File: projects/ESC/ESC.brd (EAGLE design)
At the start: 139.7 x 38.1 mm, 91 parts, among them J1 1755529, J2 1755529, J3 1755529, J4 1755529, U1 STM32F405RGT6, U10 CSD88584Q5DCT, U11 CSD88584Q5DCT, U12 CSD88584Q5DCT, U13 CSD88584Q5DCT, U2 CSD88584Q5DCT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

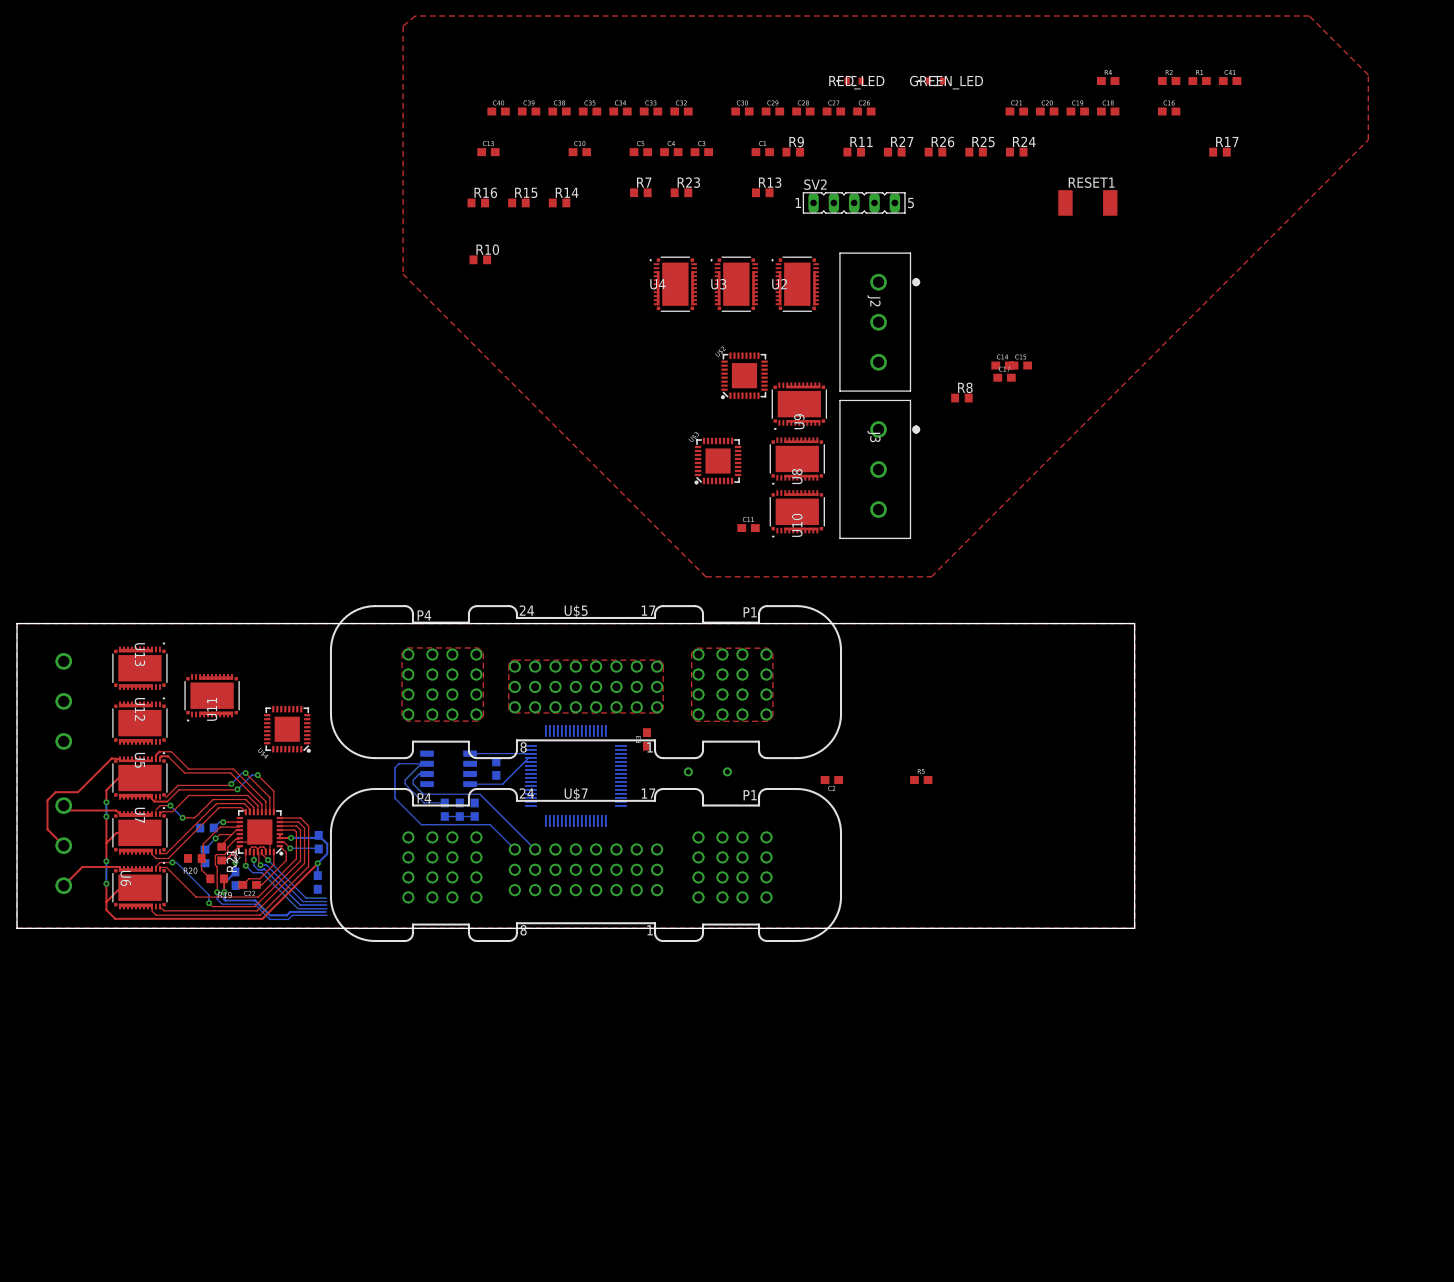
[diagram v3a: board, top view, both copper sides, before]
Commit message: finished the left half of the board
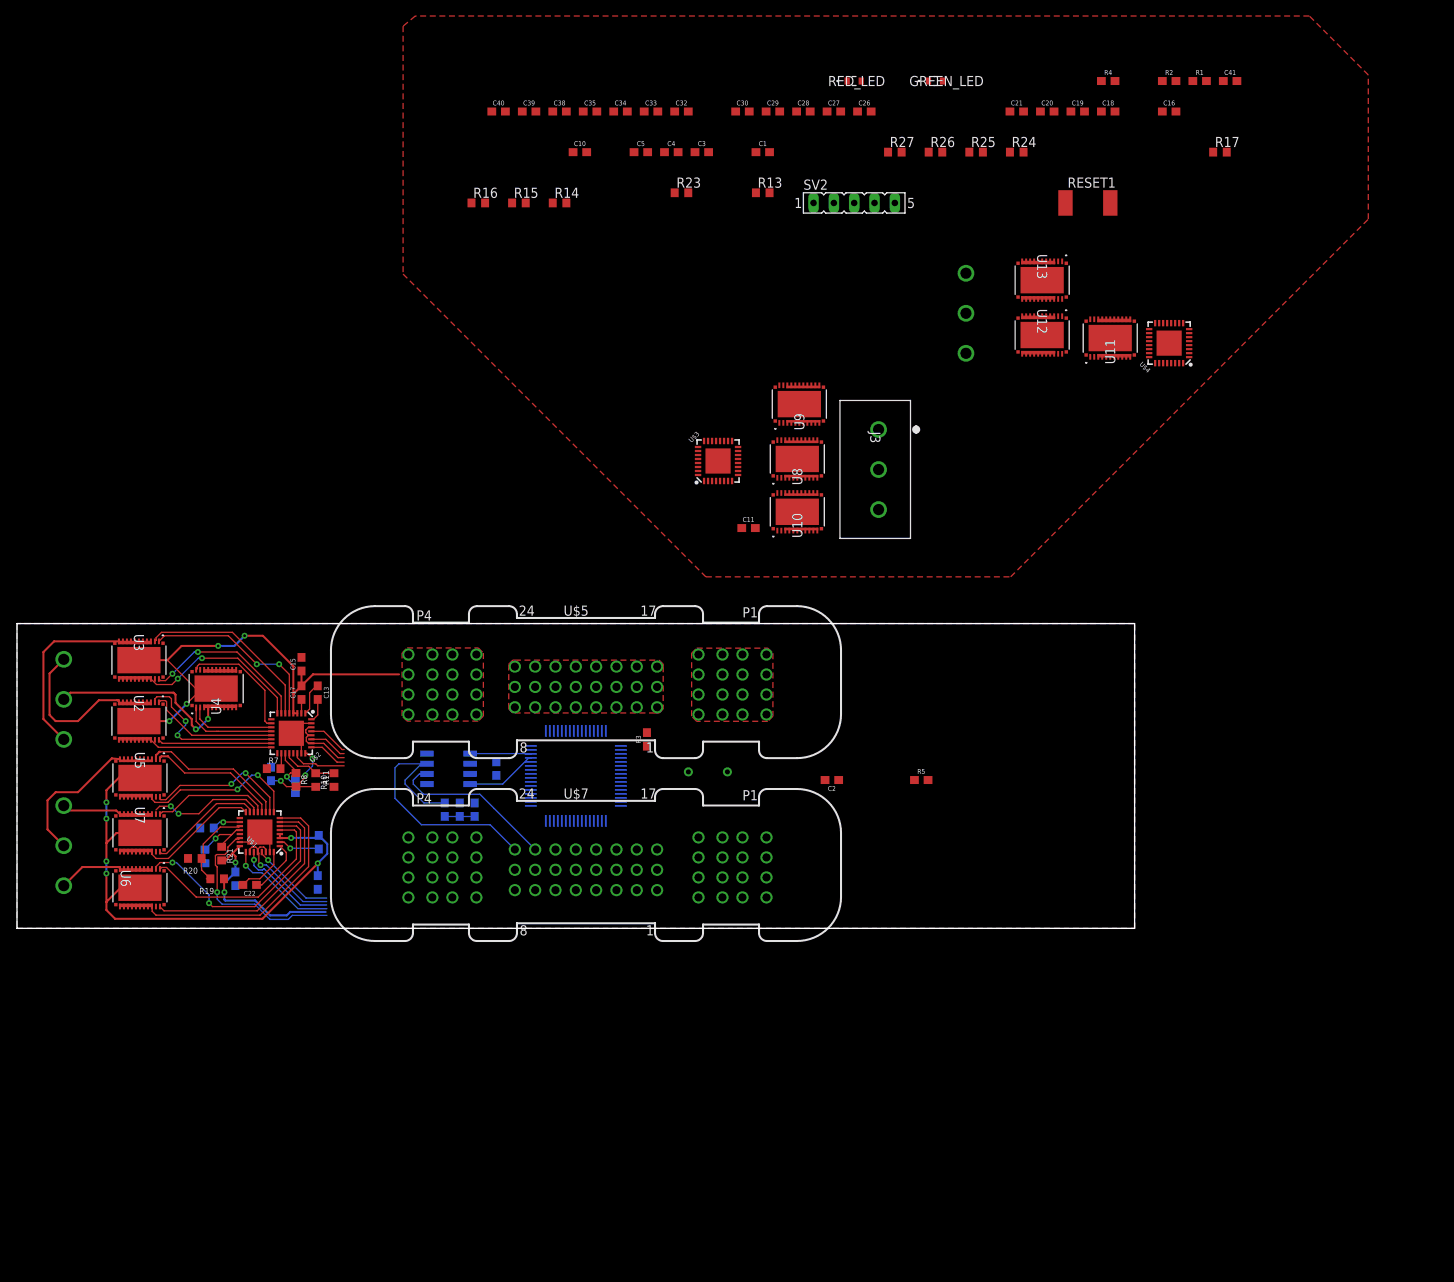
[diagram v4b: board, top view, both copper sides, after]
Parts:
- moved J4 122.8 mm to (118.6, 71.9)
- moved U12 122.8 mm to (128.1, 74.2)
- moved U13 122.8 mm to (128.1, 81.0)
- moved U11 120.8 mm to (136.7, 73.8)
- moved U$4 120.3 mm to (144.0, 73.2)
- moved J2 116.8 mm to (5.84, 23.6), flipped to the bottom, turned to 90 degrees
- moved C14 104.7 mm to (31.8, 19.3), flipped to the bottom, turned to 90 degrees
- moved R11 101.9 mm to (39.6, 18.5), turned to 90 degrees
- moved R9 100.8 mm to (34.8, 17.8), flipped to the bottom, turned to 90 degrees
- moved U2 98.8 mm to (15.2, 25.9), turned to 270 degrees
- moved C15 97.4 mm to (35.6, 33.0), turned to 90 degrees
- moved C17 96.3 mm to (35.6, 29.5), turned to 90 degrees
- moved R8 95.9 mm to (34.9, 18.6), turned to 270 degrees
- moved U3 88.2 mm to (15.2, 33.5), turned to 270 degrees
- moved R7 85.4 mm to (32.1, 20.0)
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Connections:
- removed net N$10: U$2.25
- removed net N$11: U$2.27
- removed net N$14: U$2.29
- removed net N$20: U$3.25
- removed net N$21: U$3.27
- removed net N$22: U$3.29
- net INHA_1: now also U$2.25
- net INHA_3: now also U$3.25
- net INHB_1: now also U$2.27
- net INHB_3: now also U$3.27
- net INHC_1: now also U$2.29
- net INHC_3: now also U$3.29
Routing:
- net VM_1: track 0.00 -> 64.5 mm, vias 0 -> 4
- net PHASE_B1: track 0.00 -> 27.3 mm, vias 0 -> 2
- net PHASE_A1: track 0.00 -> 26.0 mm
- net SLA_1: track 0.00 -> 25.5 mm, vias 0 -> 2
- net GHA_1: track 0.00 -> 23.5 mm, vias 0 -> 2
- net SHA_1: track 0.00 -> 23.2 mm
- net PHASE_C1: track 0.00 -> 21.8 mm
- net GLA_1: track 0.00 -> 21.3 mm, vias 0 -> 2
- net SHC_1: track 0.00 -> 20.4 mm, vias 0 -> 2
- net SLC_1: track 0.00 -> 19.4 mm
- net GHC_1: track 0.00 -> 16.5 mm
- net GLB_1: track 0.00 -> 15.2 mm
- net GLC_1: track 0.00 -> 14.2 mm
- net GHB_1: track 0.00 -> 12.1 mm
- net DVDD_1: track 0.00 -> 11.4 mm, vias 0 -> 3
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
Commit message: Added Fault connection from drvs to stm
forgot to do this earlier
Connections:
- net FAULT_1: now also U$2.17
- net FAULT_2: now also U$1.17
- net FAULT_3: now also U$3.17
- net FAULT_4: now also U$4.17
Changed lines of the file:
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@@
 <?xml version="1.0" encoding="utf-8"?>
 <!DOCTYPE eagle SYSTEM "eagle.dtd">
-<eagle version="9.4.1">
+<eagle version="9.5.1">
 <drawing>
 <settings>
@@
 <signal name="FAULT_1">
 <contactref element="U1" pad="38"/>
+<contactref element="U$2" pad="17"/>
+<wire x1="32.54" y1="21.884" x2="71.1" y2="13.4239" width="0" layer="19" extent="1-16"/>
 </signal>
 <signal name="EN_1">
@@
 <signal name="FAULT_2">
 <contactref element="U1" pad="44"/>
+<contactref element="U$1" pad="17"/>
+<wire x1="27.853" y1="13.7896" x2="68.1" y2="13.4239" width="0" layer="19" extent="1-16"/>
 </signal>
 <signal name="INL_3">
@@
 <signal name="FAULT_3">
 <contactref element="U1" pad="55"/>
+<contactref element="U$3" pad="17"/>
+<wire x1="64.2239" y1="18.3" x2="89.38" y2="60.92" width="0" layer="19" extent="1-16"/>
 </signal>
 <signal name="INHA_4">
@@
 <signal name="FAULT_4">
 <contactref element="U1" pad="28"/>
+<contactref element="U$4" pad="17"/>
+<wire x1="75.4761" y1="17.3" x2="141.518" y2="74.902" width="0" layer="19" extent="1-16"/>
 </signal>
 <signal name="OSC_IN">

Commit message: ERC stuff 1
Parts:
- moved C18 139.1 mm to (116.3, -35.6)
- moved C19 139.1 mm to (112.5, -35.6)
- moved C20 139.1 mm to (108.7, -35.6)
- moved C21 139.1 mm to (104.9, -35.6)
- moved R13 130.6 mm to (121.4, -35.6)
- moved R17 110.9 mm to (113.8, -7.62)
- moved R14 106.3 mm to (76.7, -15.2)
- moved R15 106.3 mm to (71.6, -15.2)
- moved R16 106.3 mm to (66.5, -15.2)
- moved J3 96.8 mm to (141.0, -28.6)
- moved C27 91.3 mm to (107.4, 10.9), turned to 90 degrees
- moved U8 90.1 mm to (128.0, -26.2)
- moved R23 86.2 mm to (126.5, 17.5)
- moved U9 85.5 mm to (119.1, -17.3)
- moved C26 84.5 mm to (119.9, 18.8), turned to 180 degrees
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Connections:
- removed net N$37: U$4.25
- removed net N$38: U$4.27
- removed net N$39: U$4.29
- removed net SLC_1B: U4.12, U4.13, U4.14, U4.15, U4.16, U4.17, U4.18, U4.19, U4.20
- net INHA_4: now also U$4.25
- net INHB_4: now also U$4.27
- net INHC_2: now also U$1.29
- net INHC_3: no longer U$1.29
- net INHC_4: now also U$4.29
- net SLB_1: now also U4.12, U4.13, U4.14, U4.15, U4.16, U4.17, U4.18, U4.19, U4.20
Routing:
- net INHC_3: track 10.6 -> 0.00 mm, vias 1 -> 0
- net INHC_2: track 0.00 -> 10.6 mm, vias 0 -> 1
- net SLC_1B: track 4.00 -> 0.00 mm
- net SLB_1: track 0.00 -> 4.00 mm
- added copper zone on layer 1, net N$10

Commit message: did some layout stuff
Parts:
- moved C28 17.4 mm to (125.2, 22.6)
- moved R23 17.1 mm to (112.0, 26.7), flipped to the bottom, turned to 270 degrees
- moved R25 15.7 mm to (105.2, 31.8), flipped to the bottom, turned to 270 degrees
- moved C27 9.86 mm to (109.5, 20.6), flipped to the bottom, turned to 0 degrees
- moved R27 4.44 mm to (105.2, 21.6), flipped to the bottom, turned to 90 degrees
- moved R26 3.78 mm to (105.2, 24.6), flipped to the bottom, turned to 90 degrees
- moved U12 3.70 mm to (126.2, 29.3), turned to 180 degrees
- moved U13 3.45 mm to (110.7, 33.4), turned to 180 degrees
- moved U11 3.01 mm to (118.5, 31.5), turned to 180 degrees
- moved C29 2.84 mm to (122.9, 22.6)
- moved R24 2.54 mm to (105.2, 28.7), flipped to the bottom
- moved C26 1.44 mm to (120.9, 19.8)
- moved U$4 1.30 mm to (116.1, 22.6)
- moved J4 0.72 mm to (135.1, 23.9)
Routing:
- net VM_4: track 0.00 -> 61.4 mm, vias 0 -> 4
- net PHASE_C4: track 4.00 -> 26.9 mm
- net 12V: track 0.15 -> 18.6 mm
- net INL_4: track 0.00 -> 17.6 mm, vias 0 -> 1
- net EN_4: track 0.00 -> 17.4 mm, vias 0 -> 1
- net SHA_4: track 0.00 -> 17.0 mm
- net INHC_4: track 0.00 -> 16.6 mm, vias 0 -> 1
- net PHASE_B4: track 4.00 -> 20.4 mm
- net FAULT_4: track 0.00 -> 16.1 mm, vias 0 -> 1
- net DVDD_4: track 0.00 -> 15.5 mm, vias 0 -> 1
- net GHA_4: track 0.00 -> 13.5 mm, vias 0 -> 2
- net SLC_4: track 4.00 -> 17.2 mm
- net INHB_4: track 0.00 -> 12.9 mm, vias 0 -> 1
- net N$43: track 0.00 -> 12.6 mm, vias 0 -> 1
- net GLC_4: track 0.00 -> 11.9 mm
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
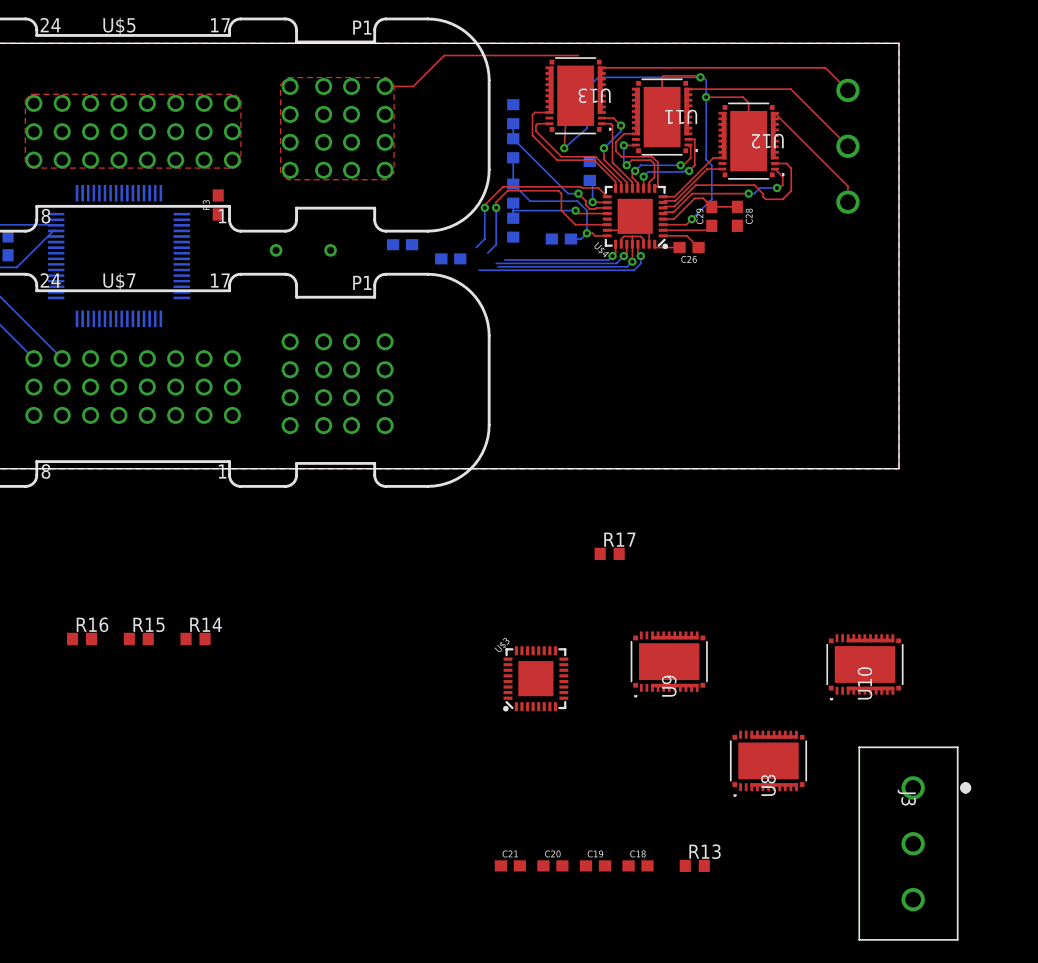
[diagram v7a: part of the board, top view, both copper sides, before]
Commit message: Did the right side of the board (needs polygons)
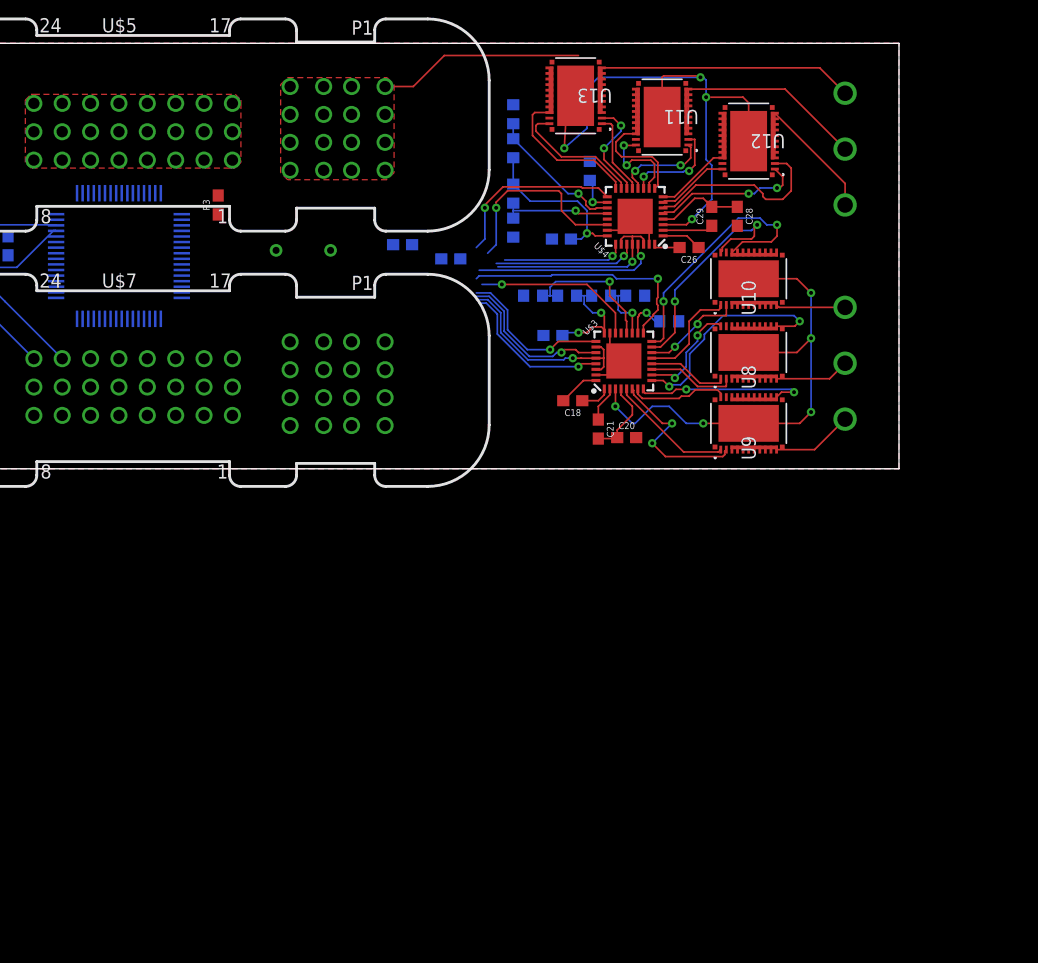
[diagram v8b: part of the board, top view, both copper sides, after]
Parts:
- moved R15 54.0 mm to (116.1, 15.5), flipped to the bottom
- moved R16 53.2 mm to (110.0, 15.5), flipped to the bottom, turned to 180 degrees
- moved R13 48.8 mm to (119.1, 13.2), flipped to the bottom
- moved C19 47.7 mm to (108.7, 11.9), flipped to the bottom
- moved R14 47.6 mm to (113.0, 15.5), flipped to the bottom
- moved C18 42.1 mm to (110.5, 6.10), turned to 180 degrees
- moved C21 39.9 mm to (112.8, 3.56), turned to 270 degrees
- moved C20 38.9 mm to (115.3, 2.79)
- moved U8 36.6 mm to (126.2, 10.4)
- moved U10 36.1 mm to (126.2, 17.0)
- moved J3 33.6 mm to (134.9, 4.45), flipped to the bottom, turned to 90 degrees
- moved U$3 29.5 mm to (115.1, 9.65)
- moved R17 24.1 mm to (106.9, 15.5), flipped to the bottom, turned to 180 degrees
- moved U9 22.5 mm to (126.2, 4.06)
- moved J4 0.36 mm to (134.9, 23.6)
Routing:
- net VM_3: track 0.00 -> 52.1 mm, vias 0 -> 5
- net SLC_3: track 0.00 -> 24.1 mm, vias 0 -> 2
- net FAULT_3: track 0.00 -> 22.0 mm, vias 0 -> 1
- net GLC_3: track 0.00 -> 21.1 mm, vias 0 -> 2
- net SLB_3: track 0.00 -> 20.0 mm, vias 0 -> 2
- net INL_3: track 0.00 -> 17.9 mm, vias 0 -> 1
- net SLA_3: track 0.00 -> 15.8 mm, vias 0 -> 2
- net SHA_3: track 0.00 -> 15.2 mm, vias 0 -> 2
- net EN_3: track 0.00 -> 14.8 mm, vias 0 -> 1
- net INHB_3: track 0.00 -> 14.3 mm, vias 0 -> 1
- net INHA_3: track 0.00 -> 14.2 mm, vias 0 -> 1
- net INHC_3: track 0.00 -> 14.0 mm, vias 0 -> 1
- net N$28: track 0.00 -> 12.9 mm, vias 0 -> 1
- net GHA_3: track 0.00 -> 11.2 mm
- net DVDD_3: track 0.00 -> 10.1 mm, vias 0 -> 2
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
